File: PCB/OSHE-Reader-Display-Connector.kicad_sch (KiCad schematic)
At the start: 1 part, among them J3 Conn_01x24_MountingPin

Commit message: added footprint to connector in schematic
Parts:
- J3: footprint (none) -> FH12A_24S_0_5SH_55_:CONN24_1X24_DRC_FFC_HIR
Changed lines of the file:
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@@
 			)
 		)
-		(property "Footprint" ""
+		(property "Footprint" "FH12A_24S_0_5SH_55_:CONN24_1X24_DRC_FFC_HIR"
 			(at 92.71 67.31 0)
 			(effects

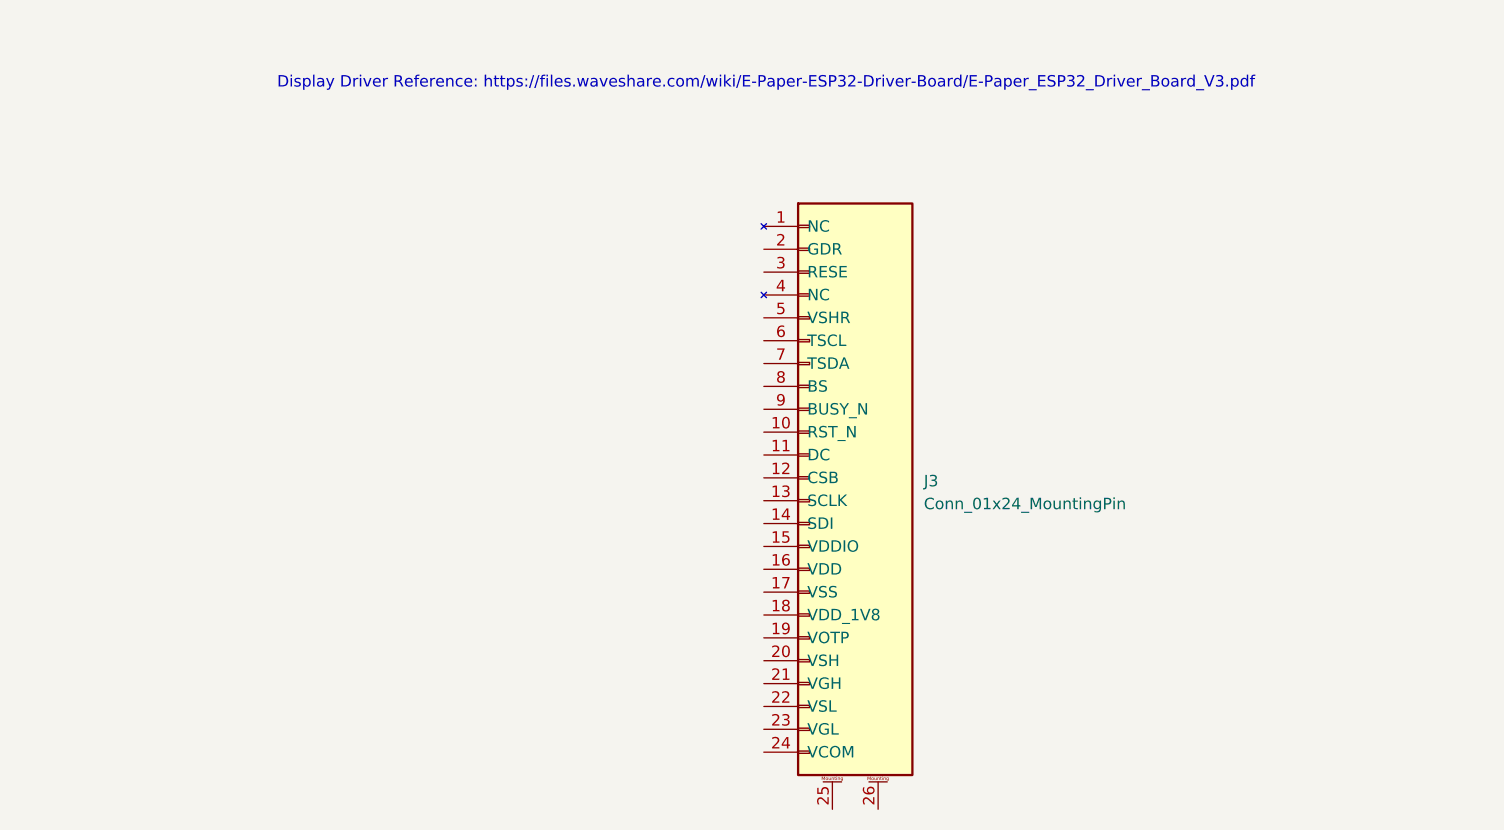
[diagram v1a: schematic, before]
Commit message: Update OSHE-Reader-Display-Connector.kicad_sch
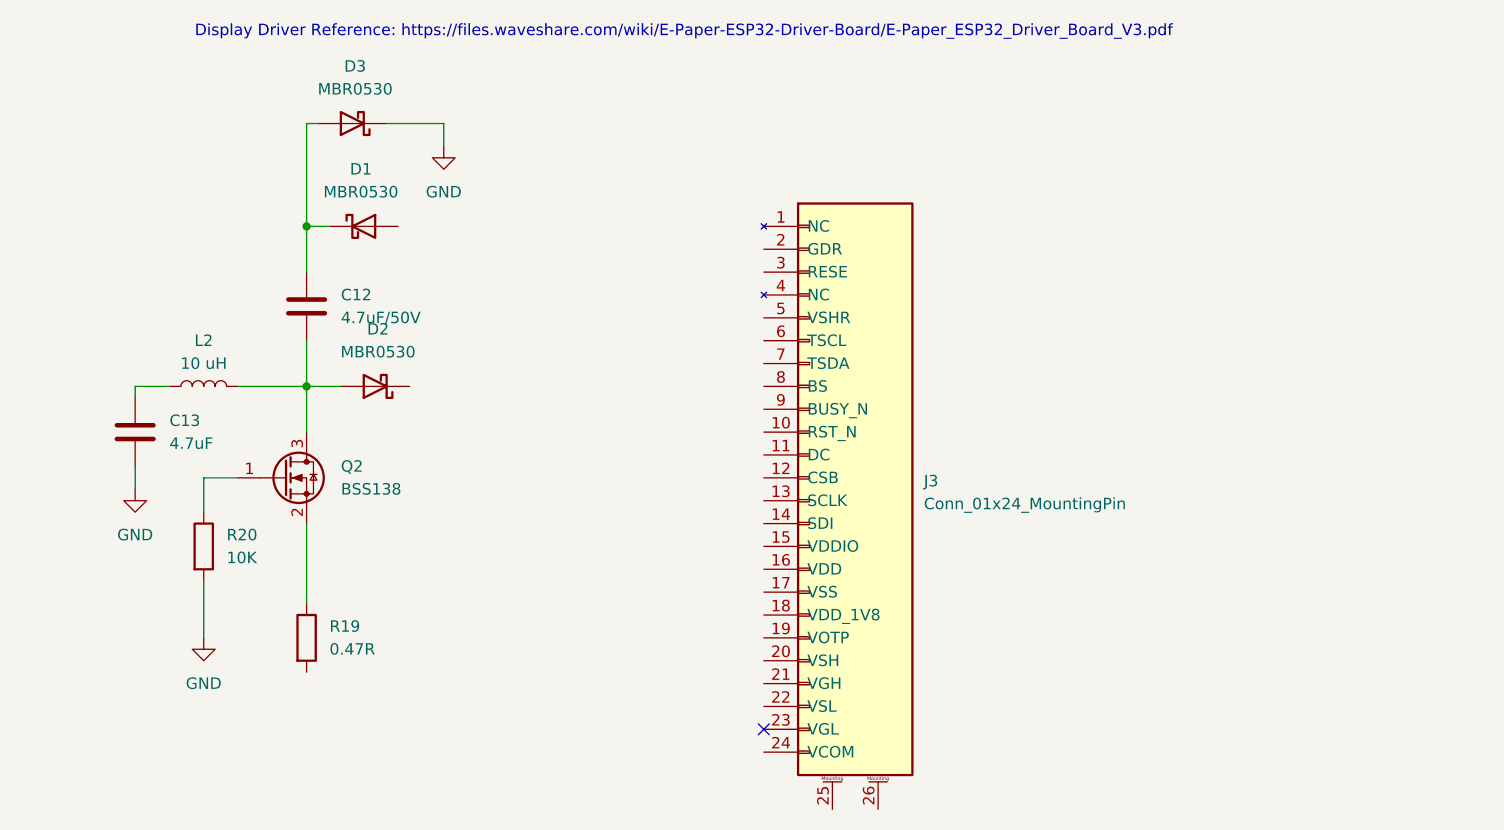
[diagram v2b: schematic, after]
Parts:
- added C12: 4.7uF/50V, symbol Device:C
- added C13: 4.7uF, symbol Device:C
- added D1, D2, D3: MBR0530, Diode_SMD:D_SOD-123, symbol Diode:MBR0530
- added L2: 10 uH, symbol Device:L
- added Q2: BSS138, Package_TO_SOT_SMD:SOT-23, symbol Transistor_FET:BSS138
- added R19: 0.47R, symbol Device:R
- added R20: 10K, symbol Device:R
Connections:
- new net: Q2.1 (G), R20.1
- new net: C12.1, D1.1 (K), D3.2 (A)
- new net: Q2.2 (S), R19.1
- new net: C12.2, D2.2 (A), L2.2, Q2.3 (D)
- new net: C13.1, L2.1
- new net GND: C13.2, D3.1 (K), R20.2
- no-connect marks 0 -> 1

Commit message: minor fixes to hierarchical aspects of sheet + slight progress on display connector
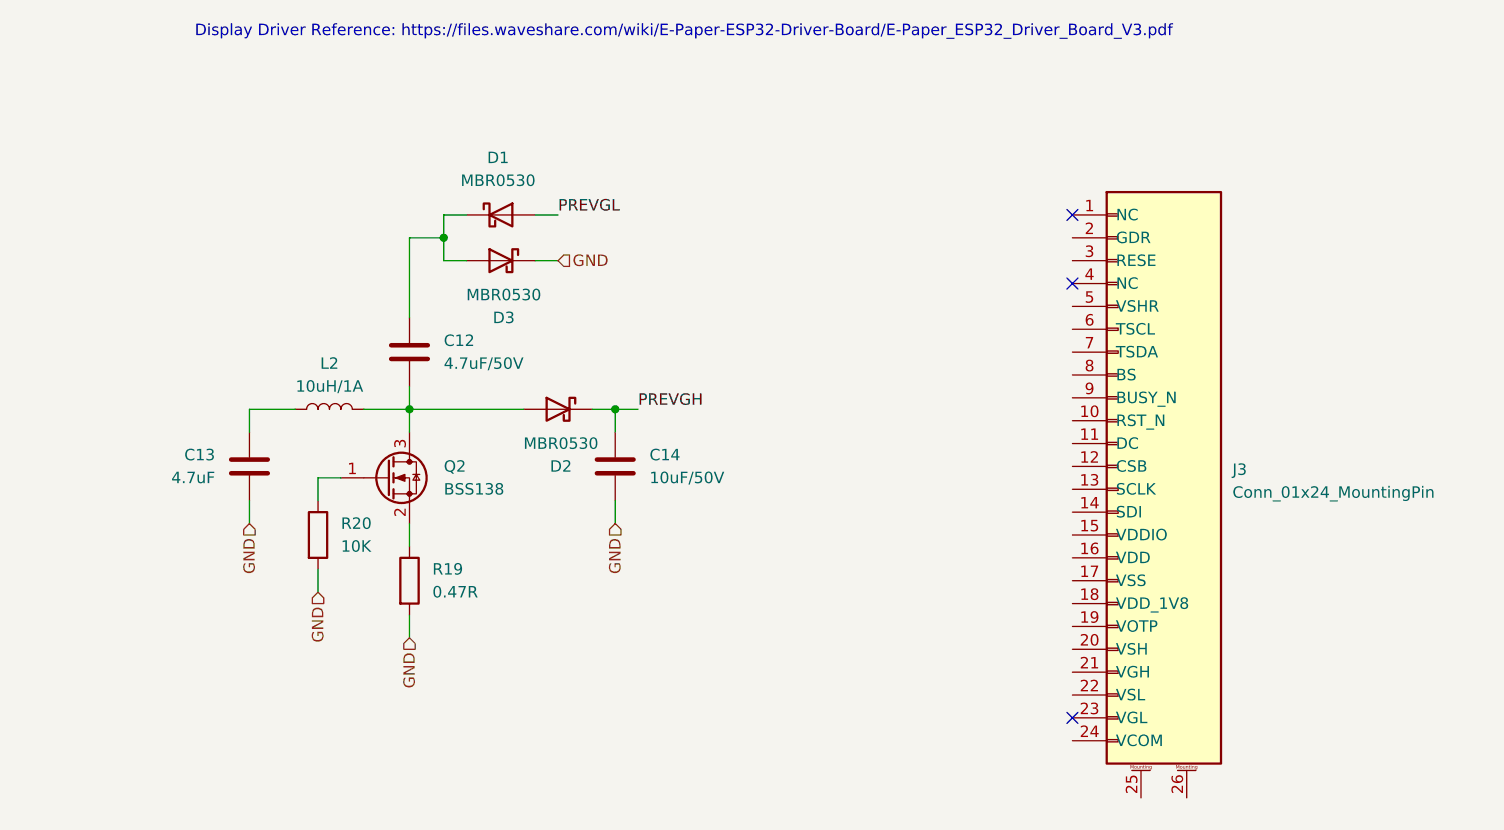
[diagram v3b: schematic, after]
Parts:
- added C14: 10uF/50V, symbol Device:C
- L2: value 10 uH -> 10uH/1A
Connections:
- net GND: now also R19.2, C14.2
- net PREVGL: now reaches D1.2 (A)
- net PREVGH: now reaches D2.1 (K)
- net PREVGH: now also C14.1
- no-connect marks 1 -> 3
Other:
- moved on the sheet: C12, C13, D1, D2, D3, L2, Q2, R19, R20

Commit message: Updates reader display connector
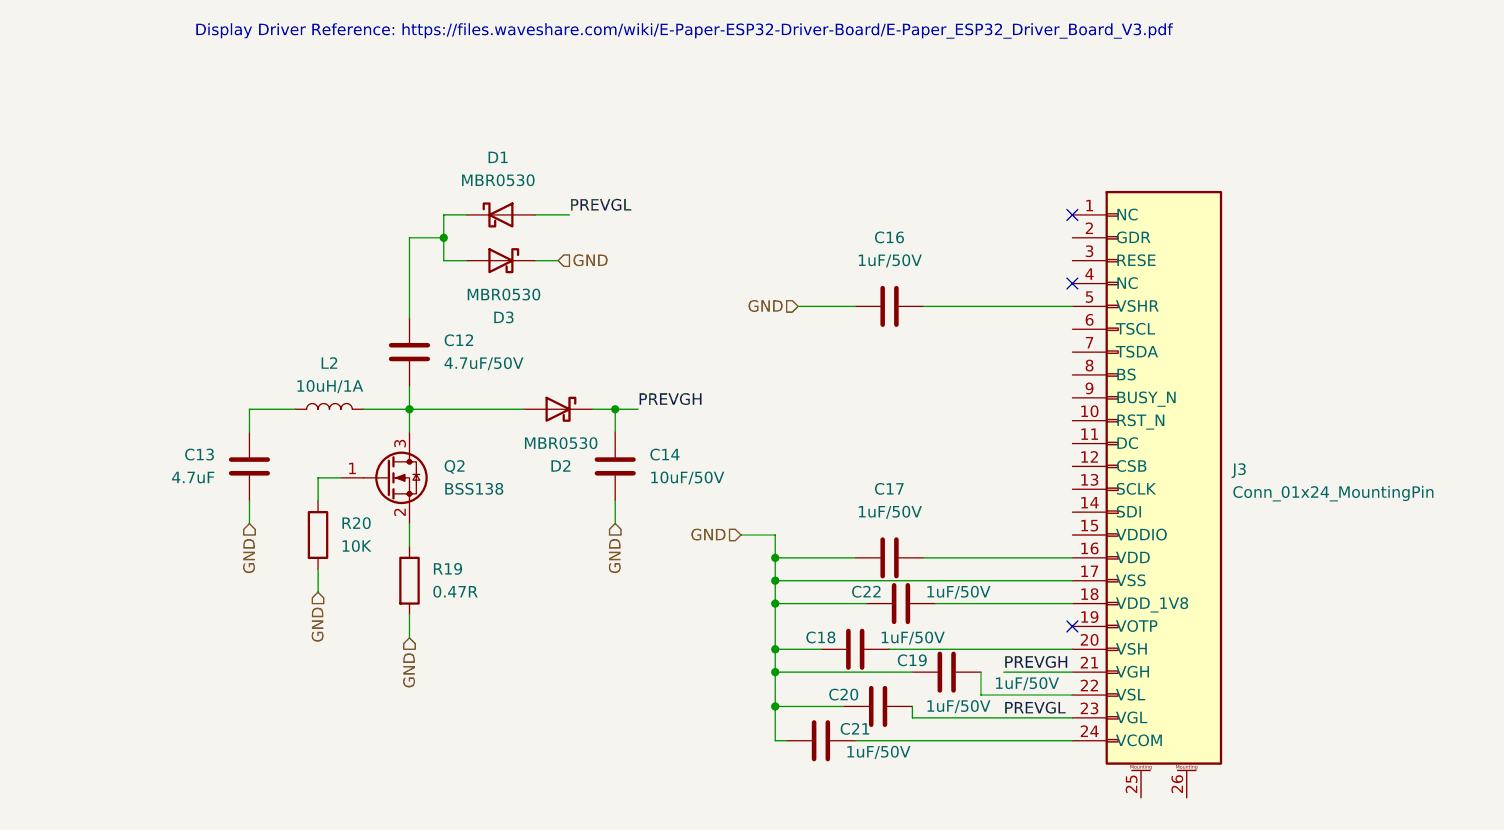
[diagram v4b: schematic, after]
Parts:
- added C16, C17, C18, C19, C20, C21, C22: 1uF/50V, symbol Device:C
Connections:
- net GND: now also J3.17 (VSS), C16.2, C17.2, C18.2, C19.2, C20.2, C21.2, C22.2
- net PREVGH: now also J3.21 (VGH)
- net PREVGL: now also J3.23 (VGL), C20.1
- net at J3.16 (VDD): now also C17.1
- net at J3.18 (VDD_1V8): now also C22.1
- net at J3.20 (VSH): now also C18.1
- net at J3.22 (VSL): now also C19.1
- net at J3.24 (VCOM): now also C21.1
- net at J3.5 (VSHR): now also C16.1

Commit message: Update OSHE-Reader-Display-Connector.kicad_sch
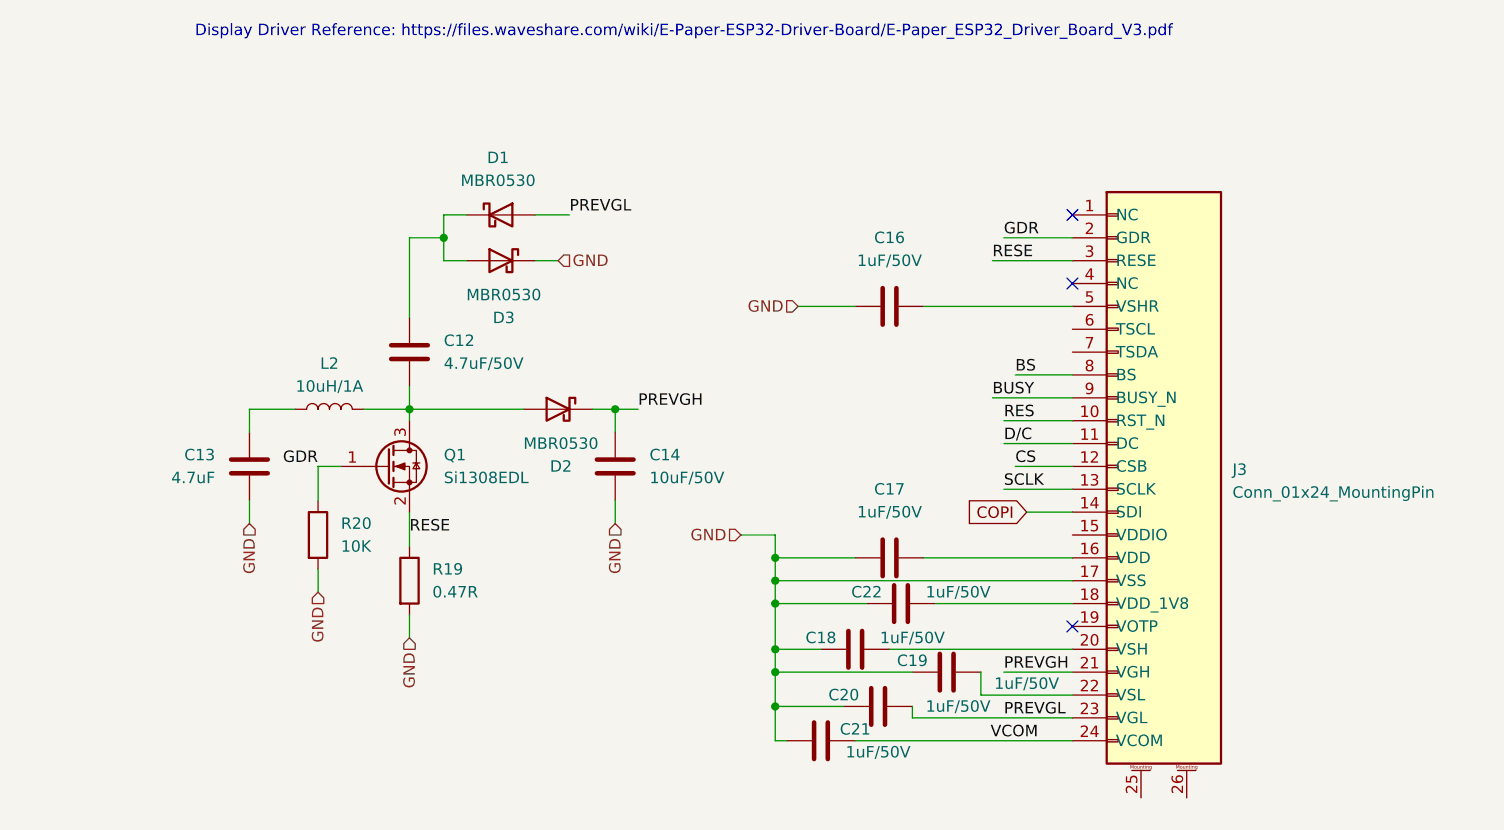
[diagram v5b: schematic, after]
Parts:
- removed Q2: BSS138, Package_TO_SOT_SMD:SOT-23, symbol Transistor_FET:BSS138
- added Q1: Si1308EDL, Package_TO_SOT_SMD:SOT-323_SC-70, symbol Transistor_FET:Si1308EDL
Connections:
- net RES: now reaches J3.10 (RST_N)
- net D/C: now reaches J3.11 (DC)
- net CS: now reaches J3.12 (CSB)
- net SCLK: now reaches J3.13 (SCLK)
- net COPI: now reaches J3.14 (SDI)
- net GDR: now reaches J3.2 (GDR)
- net GDR: now also R20.1, Q1.1 (G)
- net VCOM: now reaches C21.1, J3.24 (VCOM)
- net RESE: now reaches J3.3 (RESE)
- net RESE: now also R19.1, Q1.2 (S)
- net BS: now reaches J3.8 (BS)
- net BUSY: now reaches J3.9 (BUSY_N)
- net at C12.2, D2.2 (A), L2.2: now also Q1.3 (D)
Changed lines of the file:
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@@
 	(wire
 		(pts
-			(xy 38.1 69.85) (xy 38.1 67.31)
-		)
-		(stroke
-			(width 0)
-			(type default)
-		)
-	)
-	(wire
-		(pts
-			(xy 48.26 59.69) (xy 48.26 62.23)
+			(xy 38.1 69.85) (xy 38.1 66.04)
 		)
 		(stroke
@@
 	(wire
 		(pts
+			(xy 114.3 63.5) (xy 121.92 63.5)
+		)
+		(stroke
+			(width 0)
+			(type default)
+		)
+	)
+	(wire
+		(pts
 			(xy 88.9 81.28) (xy 99.06 81.28)
 		)
@@
 	(wire
 		(pts
+			(xy 115.57 55.88) (xy 121.92 55.88)
+		)
+		(stroke
+			(width 0)
+			(type default)
+		)
+	)
+	(wire
+		(pts
 			(xy 52.07 40.64) (xy 52.07 43.18)
 		)
@@
 	(wire
 		(pts
+			(xy 114.3 60.96) (xy 121.92 60.96)
+		)
+		(stroke
+			(width 0)
+			(type default)
+		)
+	)
+	(wire
+		(pts
+			(xy 113.03 58.42) (xy 121.92 58.42)
+		)
+		(stroke
+			(width 0)
+			(type default)
+		)
+	)
+	(wire
+		(pts
 			(xy 104.14 93.98) (xy 121.92 93.98)
 		)
@@
 	(wire
 		(pts
-			(xy 48.26 72.39) (xy 48.26 74.93)
+			(xy 48.26 71.12) (xy 48.26 74.93)
+		)
+		(stroke
+			(width 0)
+			(type default)
+		)
+	)
+	(wire
+		(pts
+			(xy 114.3 40.64) (xy 121.92 40.64)
 		)
 		(stroke
@@
 	(wire
 		(pts
-			(xy 38.1 67.31) (xy 40.64 67.31)
+			(xy 38.1 66.04) (xy 40.64 66.04)
 		)
 		(stroke
@@
 	(wire
 		(pts
+			(xy 116.84 71.12) (xy 121.92 71.12)
+		)
+		(stroke
+			(width 0)
+			(type default)
+		)
+	)
+	(wire
+		(pts
 			(xy 105.41 48.26) (xy 121.92 48.26)
 		)
@@
 	(wire
 		(pts
+			(xy 48.26 59.69) (xy 48.26 60.96)
+		)
+		(stroke
+			(width 0)
+			(type default)
+		)
+	)
+	(wire
+		(pts
+			(xy 114.3 68.58) (xy 121.92 68.58)
+		)
+		(stroke
+			(width 0)
+			(type default)
+		)
+	)
+	(wire
+		(pts
 			(xy 114.3 88.9) (xy 121.92 88.9)
 		)
@@
 	(wire
 		(pts
+			(xy 115.57 66.04) (xy 121.92 66.04)
+		)
+		(stroke
+			(width 0)
+			(type default)
+		)
+	)
+	(wire
+		(pts
+			(xy 113.03 43.18) (xy 121.92 43.18)
+		)
+		(stroke
+			(width 0)
+			(type default)
+		)
+	)
+	(wire
+		(pts
 			(xy 48.26 82.55) (xy 48.26 85.09)
 		)
@@
 			(width 0)
 			(type default)
+		)
+	)
+	(label "GDR"
+		(at 114.3 40.64 0)
+		(effects
+			(font
+				(size 1.27 1.27)
+			)
+			(justify left bottom)
+		)
+	)
+	(label "SCLK"
+		(at 114.3 68.58 0)
+		(effects
+			(font
+				(size 1.27 1.27)
+			)
+			(justify left bottom)
 		)
 	)
@@
 		)
 	)
+	(label "RESE"
+		(at 48.26 73.66 0)
+		(effects
+			(font
+				(size 1.27 1.27)
+			)
+			(justify left bottom)
+		)
+	)
+	(label "RES"
+		(at 114.3 60.96 0)
+		(effects
+			(font
+				(size 1.27 1.27)
+			)
+			(justify left bottom)
+		)
+	)
 	(label "PREVGL"
 		(at 114.3 93.98 0)
@@
 		)
 	)
+	(label "GDR"
+		(at 38.1 66.04 180)
+		(effects
+			(font
+				(size 1.27 1.27)
+			)
+			(justify right bottom)
+		)
+	)
+	(label "CS"
+		(at 115.57 66.04 0)
+		(effects
+			(font
+				(size 1.27 1.27)
+			)
+			(justify left bottom)
+		)
+	)
 	(label "PREVGL"
 		(at 66.04 38.1 0)
@@
 			)
 			(justify left bottom)
+		)
+	)
+	(label "BUSY"
+		(at 113.03 58.42 0)
+		(effects
+			(font
+				(size 1.27 1.27)
+			)
+			(justify left bottom)
+		)
+	)
+	(label "D{slash}C"
+		(at 114.3 63.5 0)
+		(effects
+			(font
+				(size 1.27 1.27)
+			)
+			(justify left bottom)
+		)
+	)
+	(label "VCOM"
+		(at 118.11 96.52 180)
+		(effects
+			(font
+				(size 1.27 1.27)
+			)
+			(justify right bottom)
+		)
+	)
+	(label "RESE"
+		(at 113.03 43.18 0)
+		(effects
+			(font
+				(size 1.27 1.27)
+			)
+			(justify left bottom)
+		)
+	)
+	(label "BS"
+		(at 115.57 55.88 0)
+		(effects
+			(font
+				(size 1.27 1.27)
+			)
+			(justify left bottom)
+		)
+	)
+	(global_label "COPI"
+		(shape input)
+		(at 116.84 71.12 180)
+		(fields_autoplaced yes)
+		(effects
+			(font
+				(size 1.27 1.27)
+			)
+			(justify right)
+		)
+		(property "Intersheetrefs" "${INTERSHEET_REFS}"
+			(at 109.3795 71.12 0)
+			(effects
+				(font
+					(size 1.27 1.27)
+				)
+				(justify right)
+				(hide yes)
+			)
 		)
 	)
@@
 	)
 	(symbol
+		(lib_id "Transistor_FET:Si1308EDL")
+		(at 45.72 66.04 0)
+		(unit 1)
+		(exclude_from_sim no)
+		(in_bom yes)
+		(on_board yes)
+		(dnp no)
+		(fields_autoplaced yes)
+		(property "Reference" "Q1"
+			(at 52.07 64.7699 0)
+			(effects
+				(font
+					(size 1.27 1.27)
+				)
+				(justify left)
+			)
+		)
+		(property "Value" "Si1308EDL"
+			(at 52.07 67.3099 0)
+			(effects
+				(font
+					(size 1.27 1.27)
+				)
+				(justify left)
+			)
+		)
+		(property "Footprint" "Package_TO_SOT_SMD:SOT-323_SC-70"
+			(at 50.8 67.945 0)
+			(effects
+				(font
+					(size 1.27 1.27)
+					(italic yes)
+				)
+				(justify left)
+				(hide yes)
+			)
+		)
+		(property "Datasheet" "https://www.vishay.com/docs/63399/si1308edl.pdf"
+			(at 50.8 69.85 0)
+			(effects
+				(font
+					(size 1.27 1.27)
+				)
+				(justify left)
+				(hide yes)
+			)
+		)
+		(property "Description" "30V Vds, 1.4A Id, N-Channel MOSFET, SC-70"
+			(at 45.72 66.04 0)
+			(effects
+				(font
+					(size 1.27 1.27)
+				)
+				(hide yes)
+			)
+		)
+		(pin "2"
+		)
+		(pin "1"
+		)
+		(pin "3"
+		)
+		(instances
+			(project ""
+				(path "/3f072c92-e35a-4654-839b-728bd3dc3a46/ab4c386c-ccef-4fd2-9471-e05e7dab2219"
+					(reference "Q1")
+					(unit 1)
+				)
+			)
+		)
+	)
+	(symbol
 		(lib_id "Diode:MBR0530")
 		(at 58.42 38.1 0)
@@
 					(unit 1)
 				)
-			)
-		)
-	)
-	(symbol
-		(lib_id "Transistor_FET:BSS138")
-		(at 45.72 67.31 0)
-		(unit 1)
-		(exclude_from_sim no)
-		(in_bom yes)
-		(on_board yes)
-		(dnp no)
-		(fields_autoplaced yes)
-		(property "Reference" "Q2"
-			(at 52.07 66.0399 0)
-			(effects
-				(font
-					(size 1.27 1.27)
-				)
-				(justify left)
-			)
-		)
-		(property "Value" "BSS138"
-			(at 52.07 68.5799 0)
-			(effects
-				(font
-					(size 1.27 1.27)
-				)
-				(justify left)
-			)
-		)
-		(property "Footprint" "Package_TO_SOT_SMD:SOT-23"
-			(at 50.8 69.215 0)
-			(effects
-				(font
-					(size 1.27 1.27)
-					(italic yes)
-				)
-				(justify left)
-				(hide yes)
-			)
-		)
-		(property "Datasheet" "https://www.onsemi.com/pub/Collateral/BSS138-D.PDF"
-			(at 50.8 71.12 0)
-			(effects
-				(font
-					(size 1.27 1.27)
-				)
-				(justify left)
-				(hide yes)
-			)
-		)
-		(property "Description" "50V Vds, 0.22A Id, N-Channel MOSFET, SOT-23"
-			(at 45.72 67.31 0)
-			(effects
-				(font
-					(size 1.27 1.27)
-				)
-				(hide yes)
-			)
-		)
-		(pin "1"
-		)
-		(pin "3"
-		)
-		(pin "2"
-		)
-		(instances
-			(project ""
-				(path "/3f072c92-e35a-4654-839b-728bd3dc3a46/ab4c386c-ccef-4fd2-9471-e05e7dab2219"
-					(reference "Q2")
-					(unit 1)
-				)
